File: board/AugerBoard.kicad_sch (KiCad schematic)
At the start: 0 parts

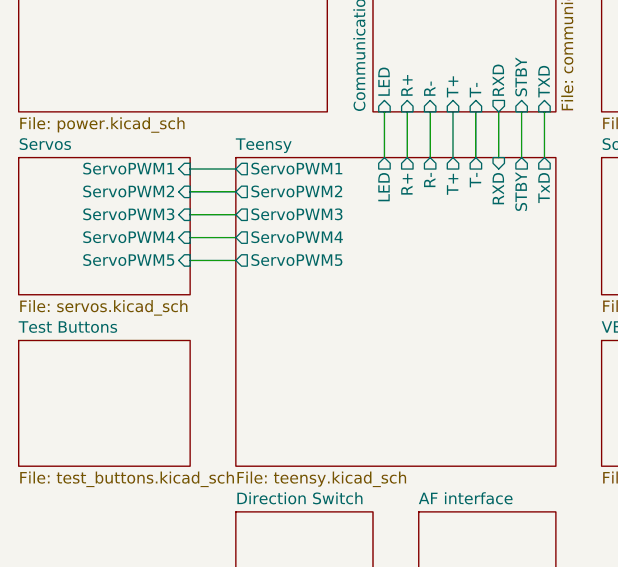
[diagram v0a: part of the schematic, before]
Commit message: Added Servo, cleaned up schematic
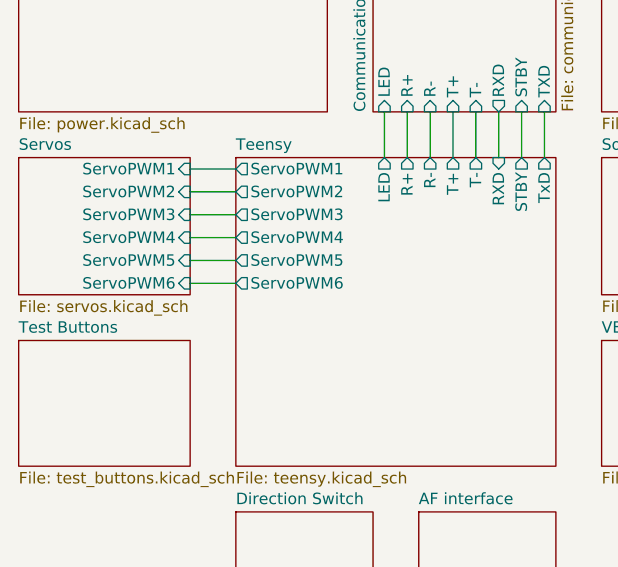
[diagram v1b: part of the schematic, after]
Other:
- sheet Servos ports: added ServoPWM6; removed none
- sheet Teensy ports: added ServoPWM6; removed none
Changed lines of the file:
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@@
+	(wire
+		(pts
+			(xy 120.65 93.98) (xy 125.73 93.98)
+		)
+		(stroke
+			(width 0)
+			(type default)
+		)
+	)
 	(wire
 		(pts
@@
 			)
 		)
+		(pin "ServoPWM6" output
+			(at 125.73 93.98 180)
+			(effects
+				(font
+					(size 1.27 1.27)
+				)
+				(justify left)
+			)
+		)
 		(instances
 			(project "AugerBoard"
@@
 			(effects
 				(font
+					(size 1.27 1.27)
+				)
+				(justify right)
+			)
+		)
+		(pin "ServoPWM6" input
+			(at 120.65 93.98 0)
+			(effects
+				(font

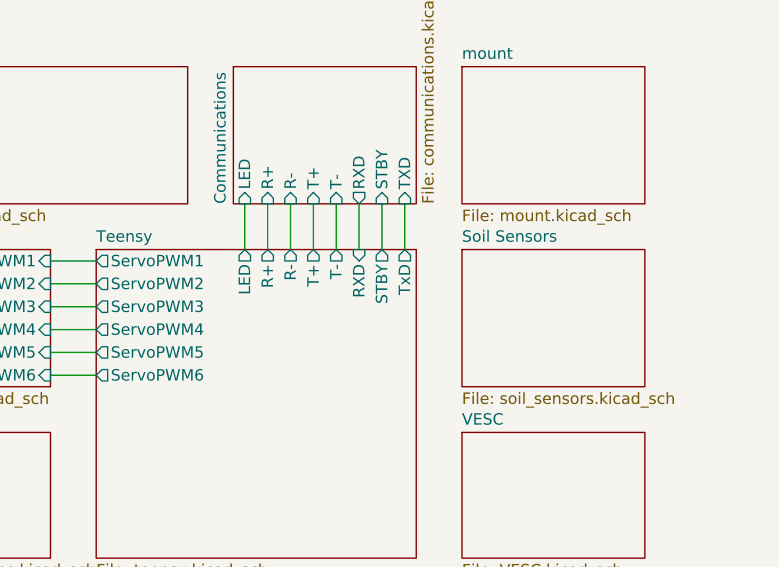
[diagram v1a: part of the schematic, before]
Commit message: Moved things to make more sense
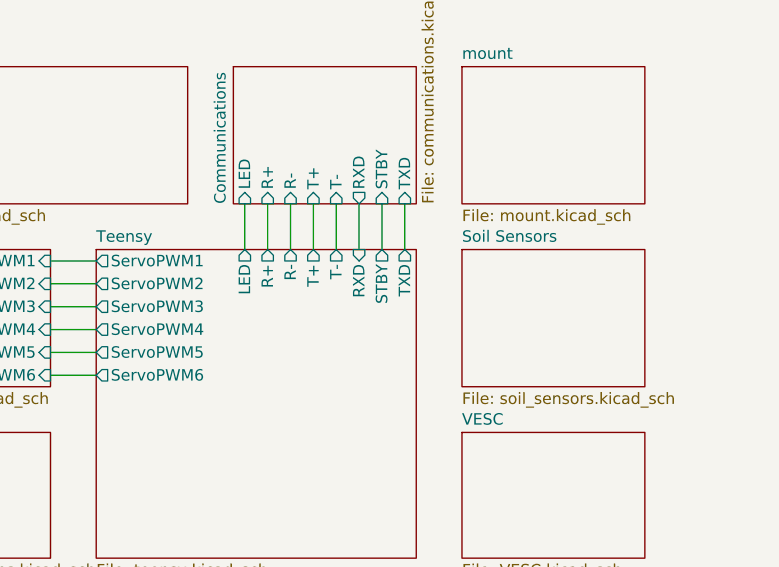
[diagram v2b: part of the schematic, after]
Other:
- sheet Teensy ports: added TXD; removed TxD
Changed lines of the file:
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@@
 			)
 		)
-		(pin "TxD" output
+		(pin "TXD" output
 			(at 160.02 80.01 90)
 			(effects

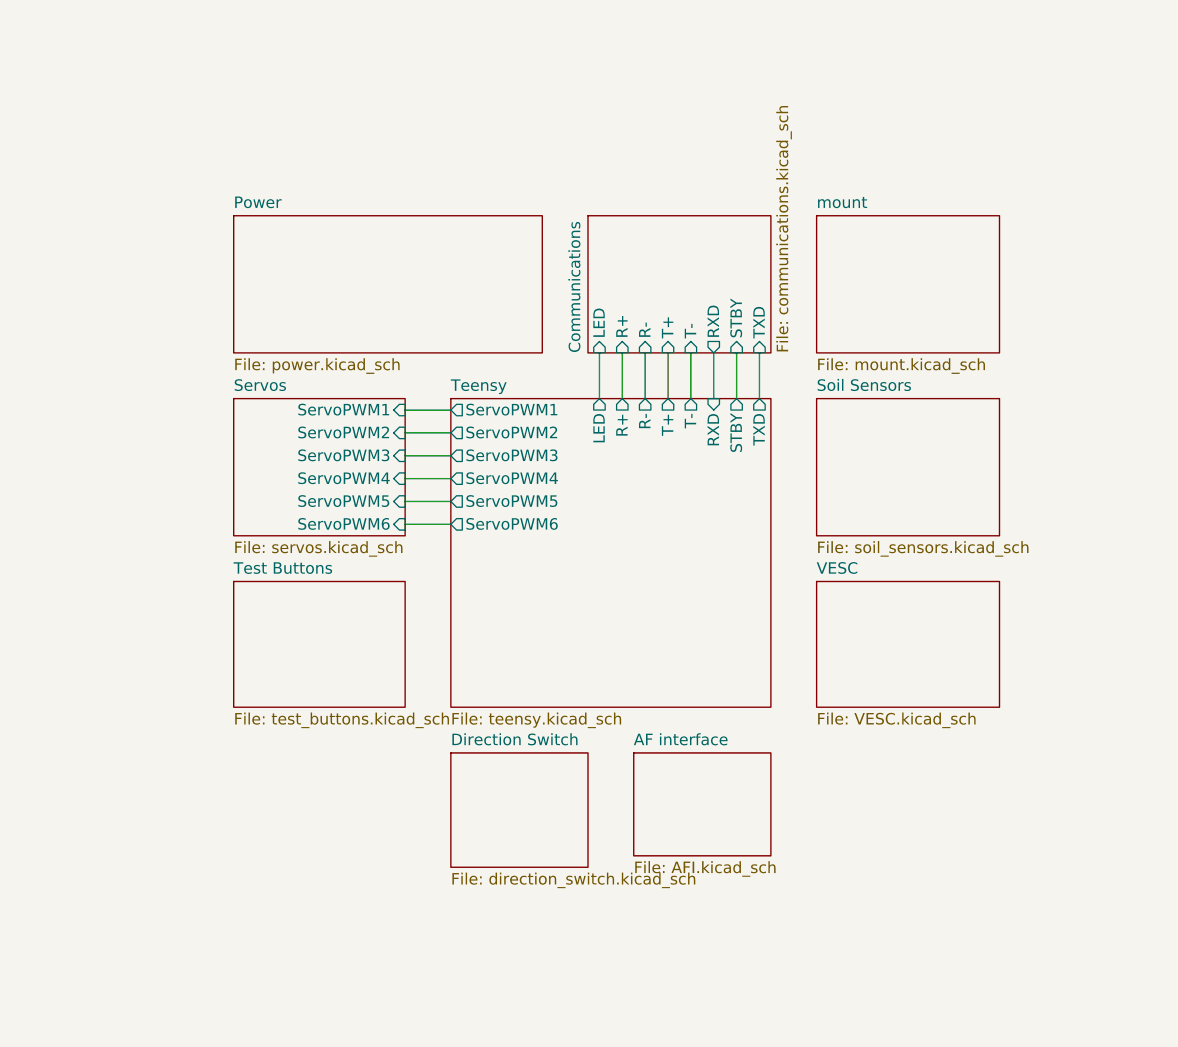
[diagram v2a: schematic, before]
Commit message: Added Parts, Renamed Parts
Added in switches, buttons, & multiple anderson connections for power.
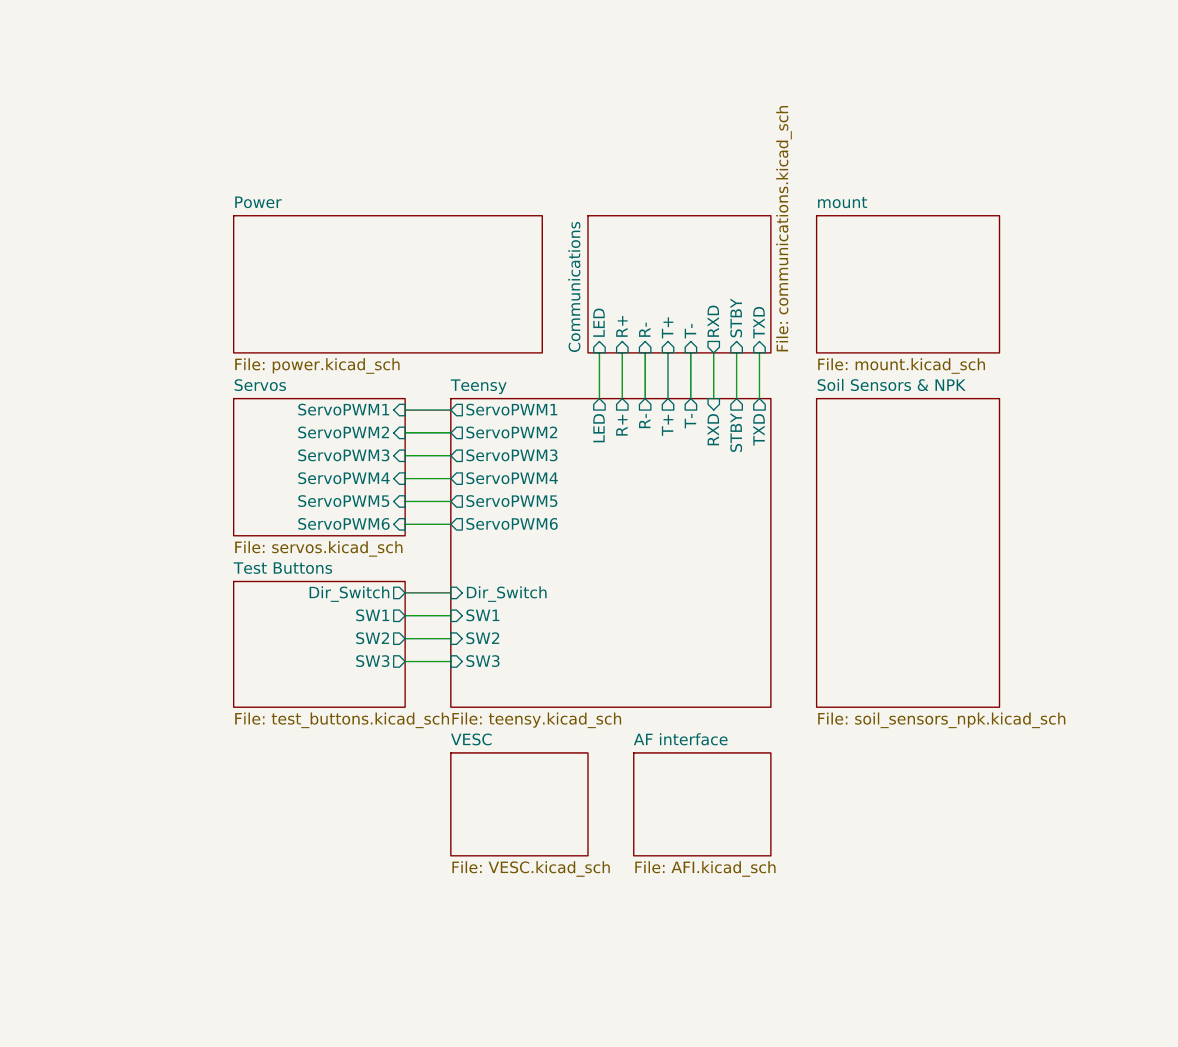
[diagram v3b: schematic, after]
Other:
- sheet Soil Sensors renamed Soil Sensors & NPK
- removed sheet Direction Switch
- sheet Soil Sensors & NPK: file soil_sensors.kicad_sch -> soil_sensors_npk.kicad_sch
- sheet Teensy ports: added Dir_Switch, SW1, SW2, SW3; removed none
- sheet Test Buttons ports: added Dir_Switch, SW1, SW2, SW3; removed none
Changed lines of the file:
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@@
+	(wire
+		(pts
+			(xy 120.65 104.14) (xy 125.73 104.14)
+		)
+		(stroke
+			(width 0)
+			(type default)
+		)
+	)
 	(wire
 		(pts
@@
 	(wire
 		(pts
+			(xy 120.65 101.6) (xy 125.73 101.6)
+		)
+		(stroke
+			(width 0)
+			(type default)
+		)
+	)
+	(wire
+		(pts
+			(xy 120.65 109.22) (xy 125.73 109.22)
+		)
+		(stroke
+			(width 0)
+			(type default)
+		)
+	)
+	(wire
+		(pts
 			(xy 154.94 74.93) (xy 154.94 80.01)
 		)
@@
 		(pts
 			(xy 147.32 74.93) (xy 147.32 80.01)
+		)
+		(stroke
+			(width 0)
+			(type default)
+		)
+	)
+	(wire
+		(pts
+			(xy 120.65 106.68) (xy 125.73 106.68)
 		)
 		(stroke
@@
 			)
 		)
+		(pin "Dir_Switch" input
+			(at 125.73 101.6 180)
+			(effects
+				(font
+					(size 1.27 1.27)
+				)
+				(justify left)
+			)
+		)
+		(pin "SW1" input
+			(at 125.73 104.14 180)
+			(effects
+				(font
+					(size 1.27 1.27)
+				)
+				(justify left)
+			)
+		)
+		(pin "SW2" input
+			(at 125.73 106.68 180)
+			(effects
+				(font
+					(size 1.27 1.27)
+				)
+				(justify left)
+			)
+		)
+		(pin "SW3" input
+			(at 125.73 109.22 180)
+			(effects
+				(font
+					(size 1.27 1.27)
+				)
+				(justify left)
+			)
+		)
 		(instances
 			(project "AugerBoard"
@@
 			)
 		)
+		(pin "Dir_Switch" output
+			(at 120.65 101.6 0)
+			(effects
+				(font
+					(size 1.27 1.27)
+				)
+				(justify right)
+			)
+		)
+		(pin "SW1" output
+			(at 120.65 104.14 0)
+			(effects
+				(font
+					(size 1.27 1.27)
+				)
+				(justify right)
+			)
+		)
+		(pin "SW2" output
+			(at 120.65 106.68 0)
+			(effects
+				(font
+					(size 1.27 1.27)
+				)
+				(justify right)
+			)
+		)
+		(pin "SW3" output
+			(at 120.65 109.22 0)
+			(effects
+				(font
+					(size 1.27 1.27)
+				)
+				(justify right)
+			)
+		)
 		(instances
 			(project "AugerBoard"
@@
 	)
 	(sheet
-		(at 166.37 100.33)
-		(size 20.32 13.97)
+		(at 125.73 119.38)
+		(size 15.24 11.43)
 		(exclude_from_sim no)
 		(in_bom yes)
@@
 		)
 		(property "Sheetname" "VESC"
-			(at 166.37 99.6184 0)
+			(at 125.73 118.6684 0)
 			(effects
 				(font
@@
 		)
 		(property "Sheetfile" "VESC.kicad_sch"
-			(at 166.37 114.8846 0)
+			(at 125.73 131.3946 0)
 			(effects
 				(font
@@
 	)
 	(sheet
-		(at 125.73 119.38)
-		(size 15.24 12.7)
+		(at 166.37 80.01)
+		(size 20.32 34.29)
 		(exclude_from_sim no)
 		(in_bom yes)
@@
 			(color 0 0 0 0.0000)
 		)
-		(property "Sheetname" "Direction Switch"
-			(at 125.73 118.6684 0)
+		(property "Sheetname" "Soil Sensors & NPK"
+			(at 166.37 79.2984 0)
 			(effects
 				(font
@@
 			)
 		)
-		(property "Sheetfile" "direction_switch.kicad_sch"
-			(at 125.73 132.6646 0)
-			(effects
-				(font
-					(size 1.27 1.27)
-				)
-				(justify left top)
-			)
-		)
-		(instances
-			(project "AugerBoard"
-				(path "/05fd3c2e-b986-4426-9c38-2a77d5c929de"
-					(page "12")
-				)
-			)
-		)
-	)
-	(sheet
-		(at 166.37 80.01)
-		(size 20.32 15.24)
-		(exclude_from_sim no)
-		(in_bom yes)
-		(on_board yes)
-		(dnp no)
-		(fields_autoplaced yes)
-		(stroke
-			(width 0.1524)
-			(type solid)
-		)
-		(fill
-			(color 0 0 0 0.0000)
-		)
-		(property "Sheetname" "Soil Sensors"
-			(at 166.37 79.2984 0)
-			(effects
-				(font
-					(size 1.27 1.27)
-				)
-				(justify left bottom)
-			)
-		)
-		(property "Sheetfile" "soil_sensors.kicad_sch"
-			(at 166.37 95.8346 0)
-			(effects
-				(font
+		(property "Sheetfile" "soil_sensors_npk.kicad_sch"
+			(at 166.37 114.8846 0)
+			(effects
+				(font

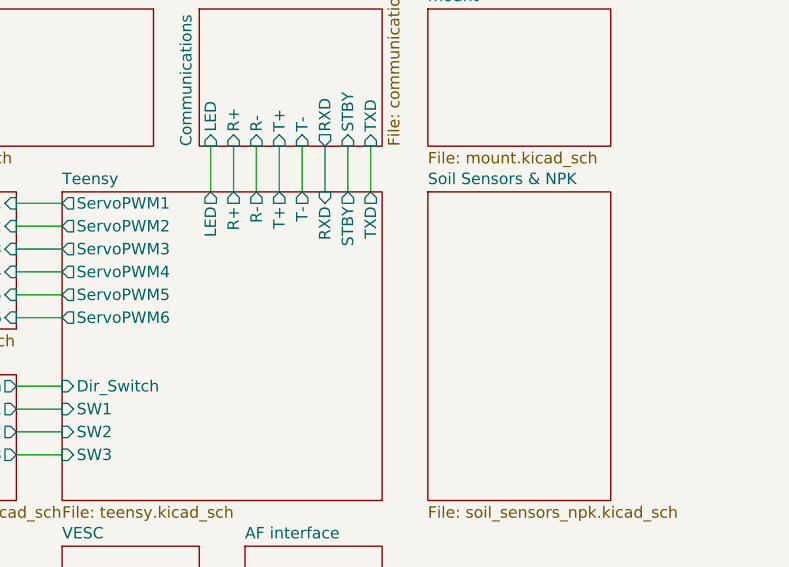
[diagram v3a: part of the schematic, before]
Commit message: added NPK and soil sensors pt. 1
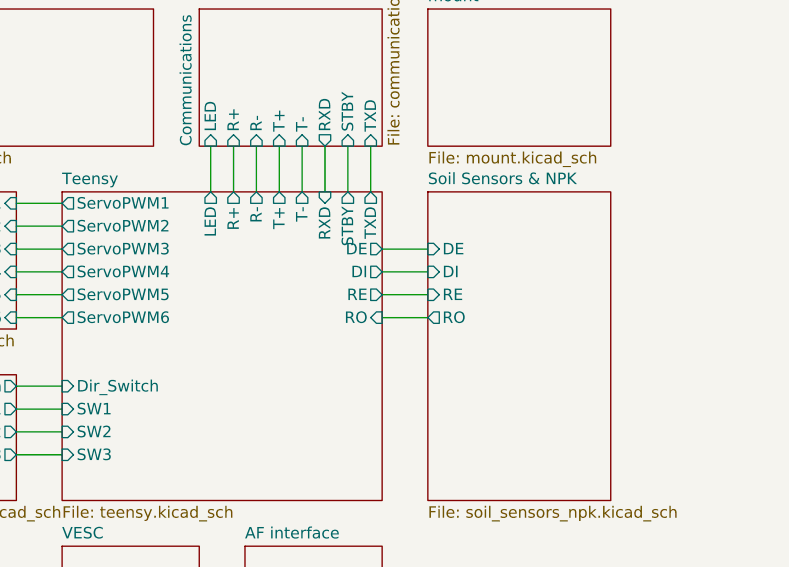
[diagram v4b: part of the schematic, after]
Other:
- sheet Soil Sensors & NPK ports: added DE, DI, RE, RO; removed none
- sheet Teensy ports: added DE, DI, RE, RO; removed none
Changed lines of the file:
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@@
+	(wire
+		(pts
+			(xy 161.29 93.98) (xy 166.37 93.98)
+		)
+		(stroke
+			(width 0)
+			(type default)
+		)
+	)
 	(wire
 		(pts
@@
 	(wire
 		(pts
+			(xy 161.29 91.44) (xy 166.37 91.44)
+		)
+		(stroke
+			(width 0)
+			(type default)
+		)
+	)
+	(wire
+		(pts
 			(xy 120.65 88.9) (xy 125.73 88.9)
 		)
@@
 		(pts
 			(xy 160.02 74.93) (xy 160.02 80.01)
+		)
+		(stroke
+			(width 0)
+			(type default)
+		)
+	)
+	(wire
+		(pts
+			(xy 161.29 86.36) (xy 166.37 86.36)
+		)
+		(stroke
+			(width 0)
+			(type default)
+		)
+	)
+	(wire
+		(pts
+			(xy 161.29 88.9) (xy 166.37 88.9)
 		)
 		(stroke
@@
 			)
 		)
+		(pin "DE" output
+			(at 161.29 86.36 0)
+			(effects
+				(font
+					(size 1.27 1.27)
+				)
+				(justify right)
+			)
+		)
+		(pin "DI" output
+			(at 161.29 88.9 0)
+			(effects
+				(font
+					(size 1.27 1.27)
+				)
+				(justify right)
+			)
+		)
+		(pin "RE" output
+			(at 161.29 91.44 0)
+			(effects
+				(font
+					(size 1.27 1.27)
+				)
+				(justify right)
+			)
+		)
+		(pin "RO" input
+			(at 161.29 93.98 0)
+			(effects
+				(font
+					(size 1.27 1.27)
+				)
+				(justify right)
+			)
+		)
 		(instances
 			(project "AugerBoard"
@@
 			)
 		)
+		(pin "DE" input
+			(at 166.37 86.36 180)
+			(effects
+				(font
+					(size 1.27 1.27)
+				)
+				(justify left)
+			)
+		)
+		(pin "DI" input
+			(at 166.37 88.9 180)
+			(effects
+				(font
+					(size 1.27 1.27)
+				)
+				(justify left)
+			)
+		)
+		(pin "RE" input
+			(at 166.37 91.44 180)
+			(effects
+				(font
+					(size 1.27 1.27)
+				)
+				(justify left)
+			)
+		)
+		(pin "RO" output
+			(at 166.37 93.98 180)
+			(effects
+				(font
+					(size 1.27 1.27)
+				)
+				(justify left)
+			)
+		)
